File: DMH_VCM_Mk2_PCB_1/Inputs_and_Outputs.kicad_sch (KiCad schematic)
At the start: 33 parts, among them J0 Conn_01x01, J1 TS_Jack_6.35mm_Sw, J10 TS_Jack_6.35mm_Sw, J2 TS_Jack_6.35mm_Sw, J200 IDC_02x05, J3 TS_Jack_6.35mm_Sw, J4 TS_Jack_6.35mm_Sw, J5 TS_Jack_6.35mm_Sw, J50 Conn_01x06, J6 TS_Jack_6.35mm_Sw, J60 Conn_01x06, J7 TS_Jack_6.35mm_Sw, J70 Conn_01x06, J8 TS_Jack_6.35mm_Sw, J9 TS_Jack_6.35mm_Sw, SW1 SW_DPDT, SW2 SW_DPDT, SW3 SW_DPDT

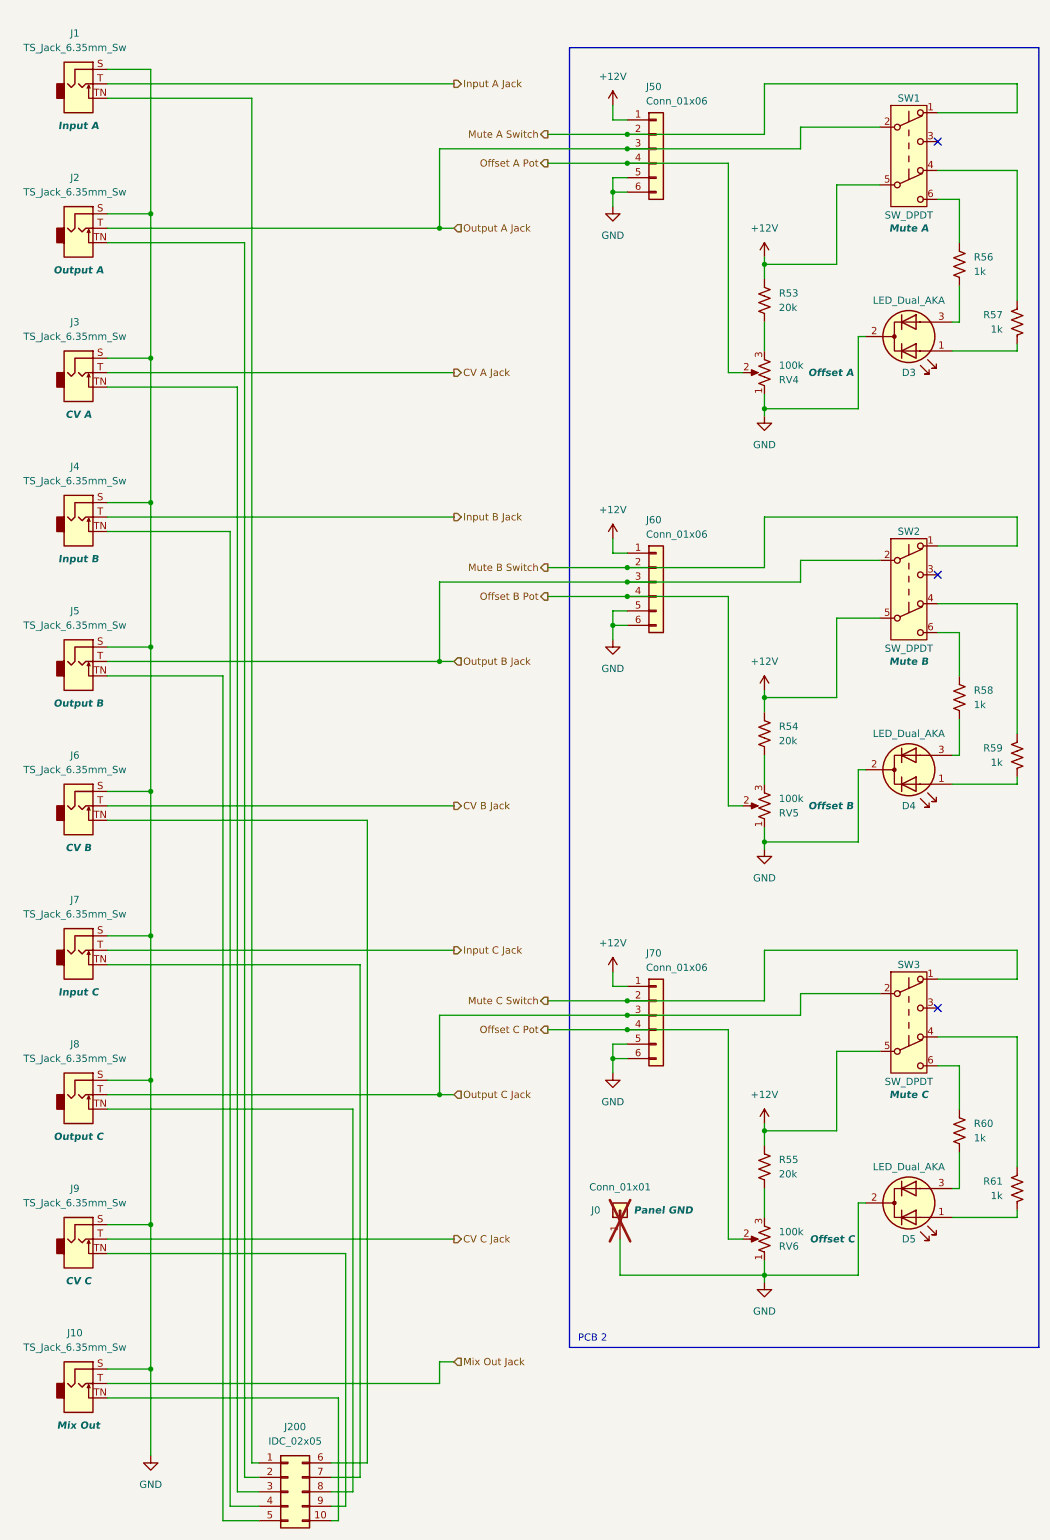
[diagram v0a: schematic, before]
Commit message: Almost finished PCB 1 schematic
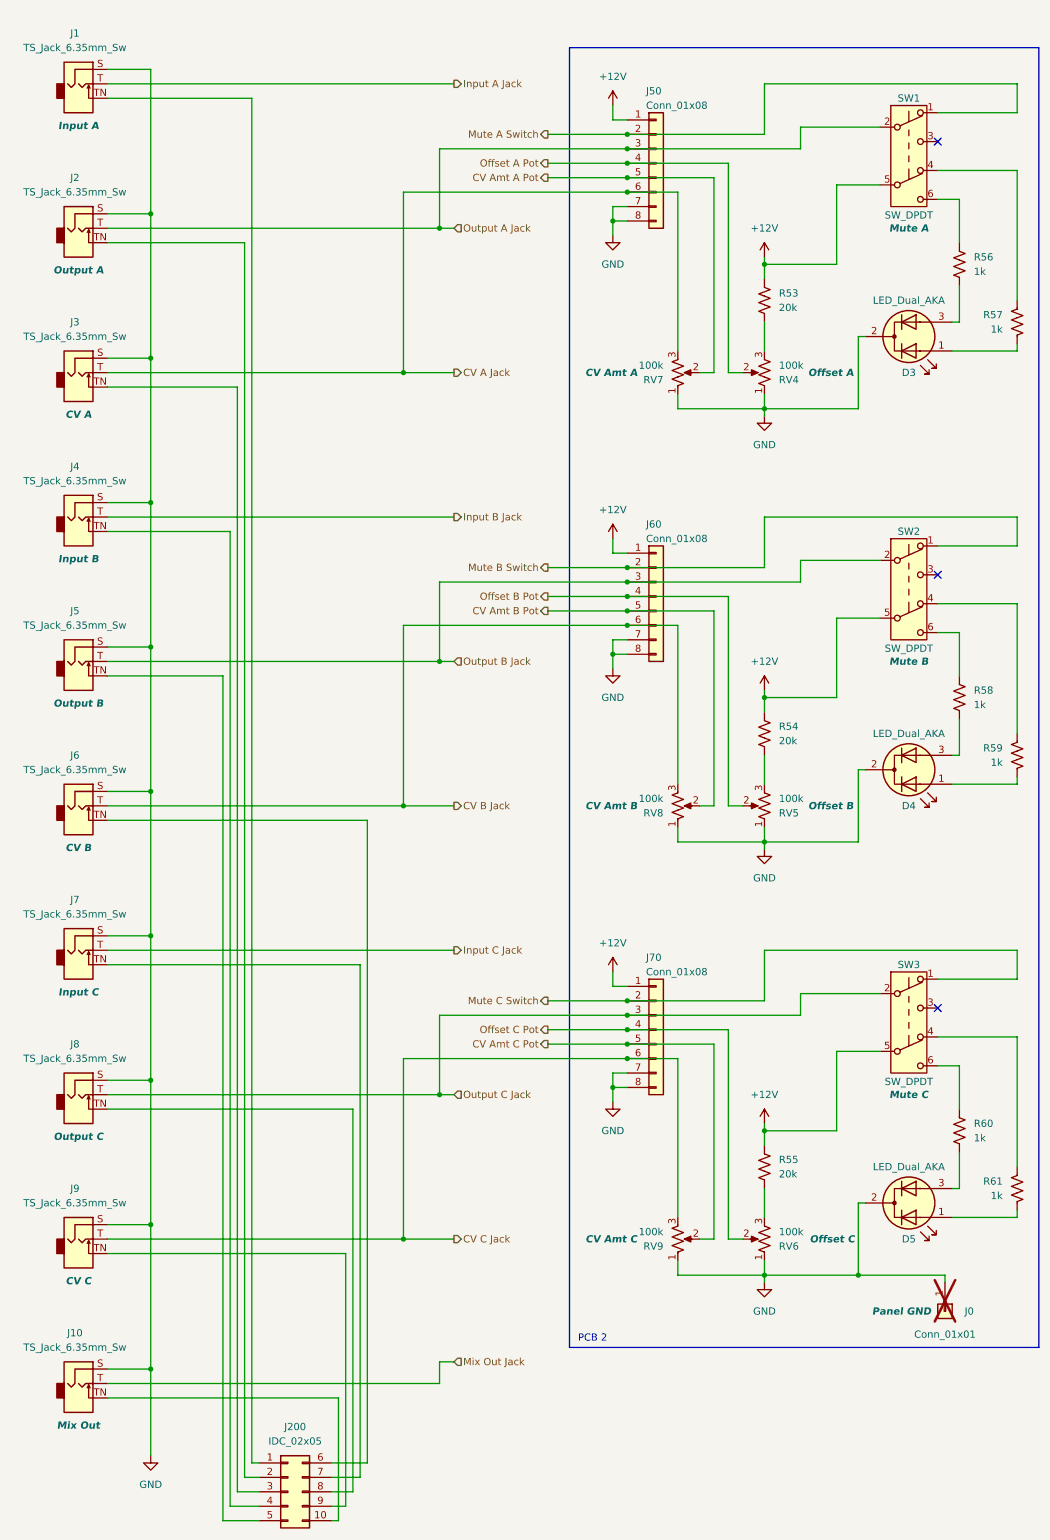
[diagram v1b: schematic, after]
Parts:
- added RV7, RV8, RV9: 100k, SynthStuff:Potentiometer_TT_P110KH1, symbol Device:R_Potentiometer_US
- J50, J60, J70: value Conn_01x06 -> Conn_01x08; symbol Connector_Generic:Conn_01x06 -> Connector_Generic:Conn_01x08
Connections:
- net CV A Jack: now also J50.6 (Pin_6), RV7.3
- net CV B Jack: now also J60.6 (Pin_6), RV8.3
- net CV C Jack: now also J70.6 (Pin_6), RV9.3
- net GND: now also J50.7 (Pin_7), J50.8 (Pin_8), J60.7 (Pin_7), J60.8 (Pin_8), J70.7 (Pin_7), J70.8 (Pin_8), RV7.1, RV8.1, RV9.1; no longer J50.5 (Pin_5), J50.6 (Pin_6), J60.5 (Pin_5), J60.6 (Pin_6), J70.5 (Pin_5), J70.6 (Pin_6)
- new net CV Amt A Pot: J50.5 (Pin_5), RV7.2
- new net CV Amt B Pot: J60.5 (Pin_5), RV8.2
- new net CV Amt C Pot: J70.5 (Pin_5), RV9.2
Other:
- moved on the sheet: J0

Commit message: PCB 1 placement in progress
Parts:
- J50, J60, J70: footprint Connector_PinSocket_2.54mm:PinSocket_1x06_P2.54mm_Vertical -> Connector_PinSocket_2.54mm:PinSocket_1x08_P2.54mm_Vertical
- SW1, SW2, SW3: footprint SynthStuff:Toggle_Switch_2_Poles_THT -> SynthStuff:Toggle_Switch_2_Poles_TE
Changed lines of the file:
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@@
 			)
 		)
-		(property "Footprint" "SynthStuff:Toggle_Switch_2_Poles_THT"
+		(property "Footprint" "SynthStuff:Toggle_Switch_2_Poles_TE"
 			(at 171.45 33.02 0)
 			(effects
@@
 			)
 		)
-		(property "Footprint" "SynthStuff:Toggle_Switch_2_Poles_THT"
+		(property "Footprint" "SynthStuff:Toggle_Switch_2_Poles_TE"
 			(at 171.45 185.42 0)
 			(effects
@@
 			)
 		)
-		(property "Footprint" "SynthStuff:Toggle_Switch_2_Poles_THT"
+		(property "Footprint" "SynthStuff:Toggle_Switch_2_Poles_TE"
 			(at 171.45 109.22 0)
 			(effects
@@
 			)
 		)
-		(property "Footprint" "Connector_PinSocket_2.54mm:PinSocket_1x06_P2.54mm_Vertical"
+		(property "Footprint" "Connector_PinSocket_2.54mm:PinSocket_1x08_P2.54mm_Vertical"
 			(at 127 115.57 0)
 			(effects
@@
 				)
 				(hide yes)
+			)
+		)
+		(property "Function" ""
+			(at 127 115.57 0)
+			(effects
+				(font
+					(size 1.27 1.27)
+				)
 			)
 		)
@@
 			)
 		)
-		(property "Footprint" "Connector_PinSocket_2.54mm:PinSocket_1x06_P2.54mm_Vertical"
+		(property "Footprint" "Connector_PinSocket_2.54mm:PinSocket_1x08_P2.54mm_Vertical"
 			(at 127 191.77 0)
 			(effects
@@
 			)
 		)
+		(property "Function" ""
+			(at 127 191.77 0)
+			(effects
+				(font
+					(size 1.27 1.27)
+				)
+			)
+		)
 		(pin "6"
 		)
@@
 			)
 		)
-		(property "Footprint" "Connector_PinSocket_2.54mm:PinSocket_1x06_P2.54mm_Vertical"
+		(property "Footprint" "Connector_PinSocket_2.54mm:PinSocket_1x08_P2.54mm_Vertical"
 			(at 127 39.37 0)
 			(effects
@@
 			)
 		)
+		(property "Function" ""
+			(at 127 39.37 0)
+			(effects
+				(font
+					(size 1.27 1.27)
+				)
+			)
+		)

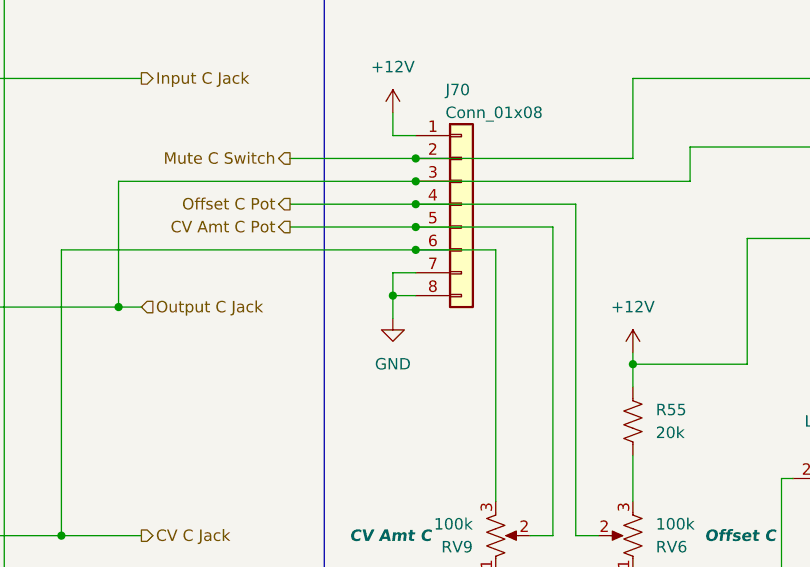
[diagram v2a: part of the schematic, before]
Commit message: Resolved J70 volume conflict
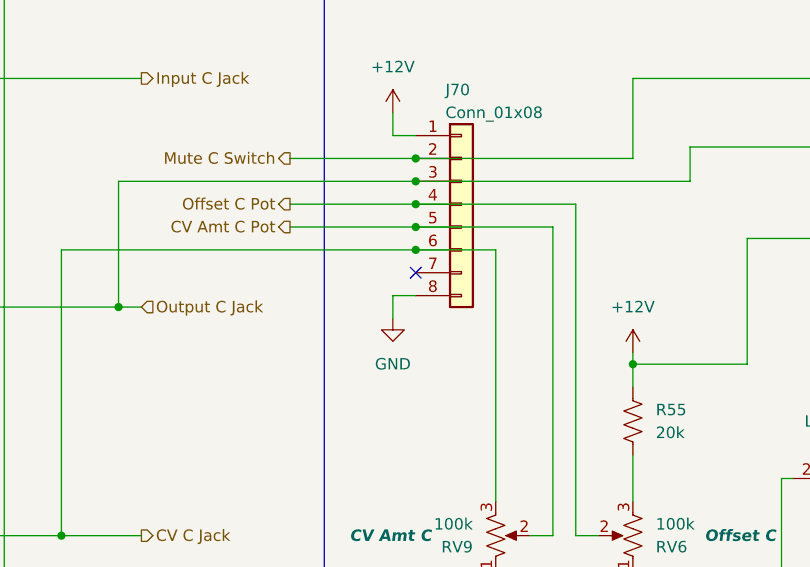
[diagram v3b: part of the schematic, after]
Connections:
- net GND: no longer J70.7 (Pin_7)
- no-connect marks 3 -> 4
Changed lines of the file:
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@@
-	)
-	(junction
-		(at 119.38 201.93)
-		(diameter 0)
-		(color 0 0 0 0)
 	)
 	(junction
@@
 		(at 176.53 35.56)
 	)
+	(no_connect
+		(at 121.92 199.39)
+	)
 	(wire
 		(pts
@@
 	(wire
 		(pts
-			(xy 119.38 199.39) (xy 119.38 201.93)
-		)
-		(stroke
-			(width 0)
-			(type default)
-		)
-	)
-	(wire
-		(pts
 			(xy 119.38 184.15) (xy 121.92 184.15)
 		)
@@
 		)
 		(stroke
-			(width 0)
-			(type default)
-		)
-	)
-	(wire
-		(pts
-			(xy 121.92 199.39) (xy 119.38 199.39)
-		)
-		(stroke

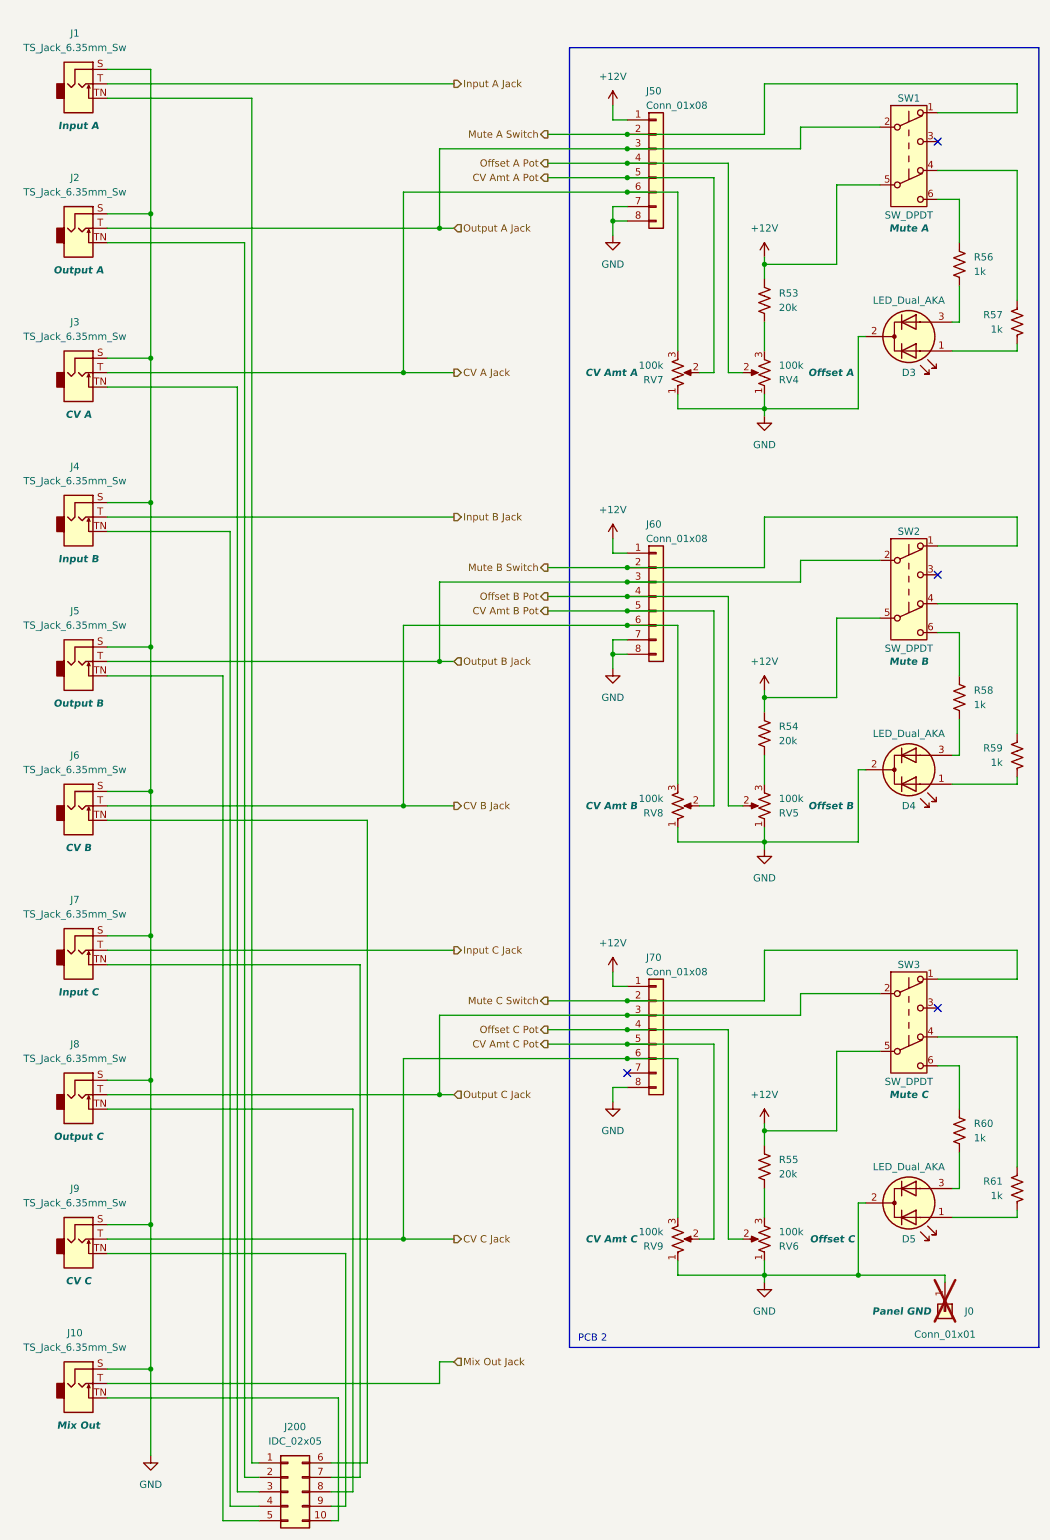
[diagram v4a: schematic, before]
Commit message: Added +/-7v5 to input TN and normalled CV inputs
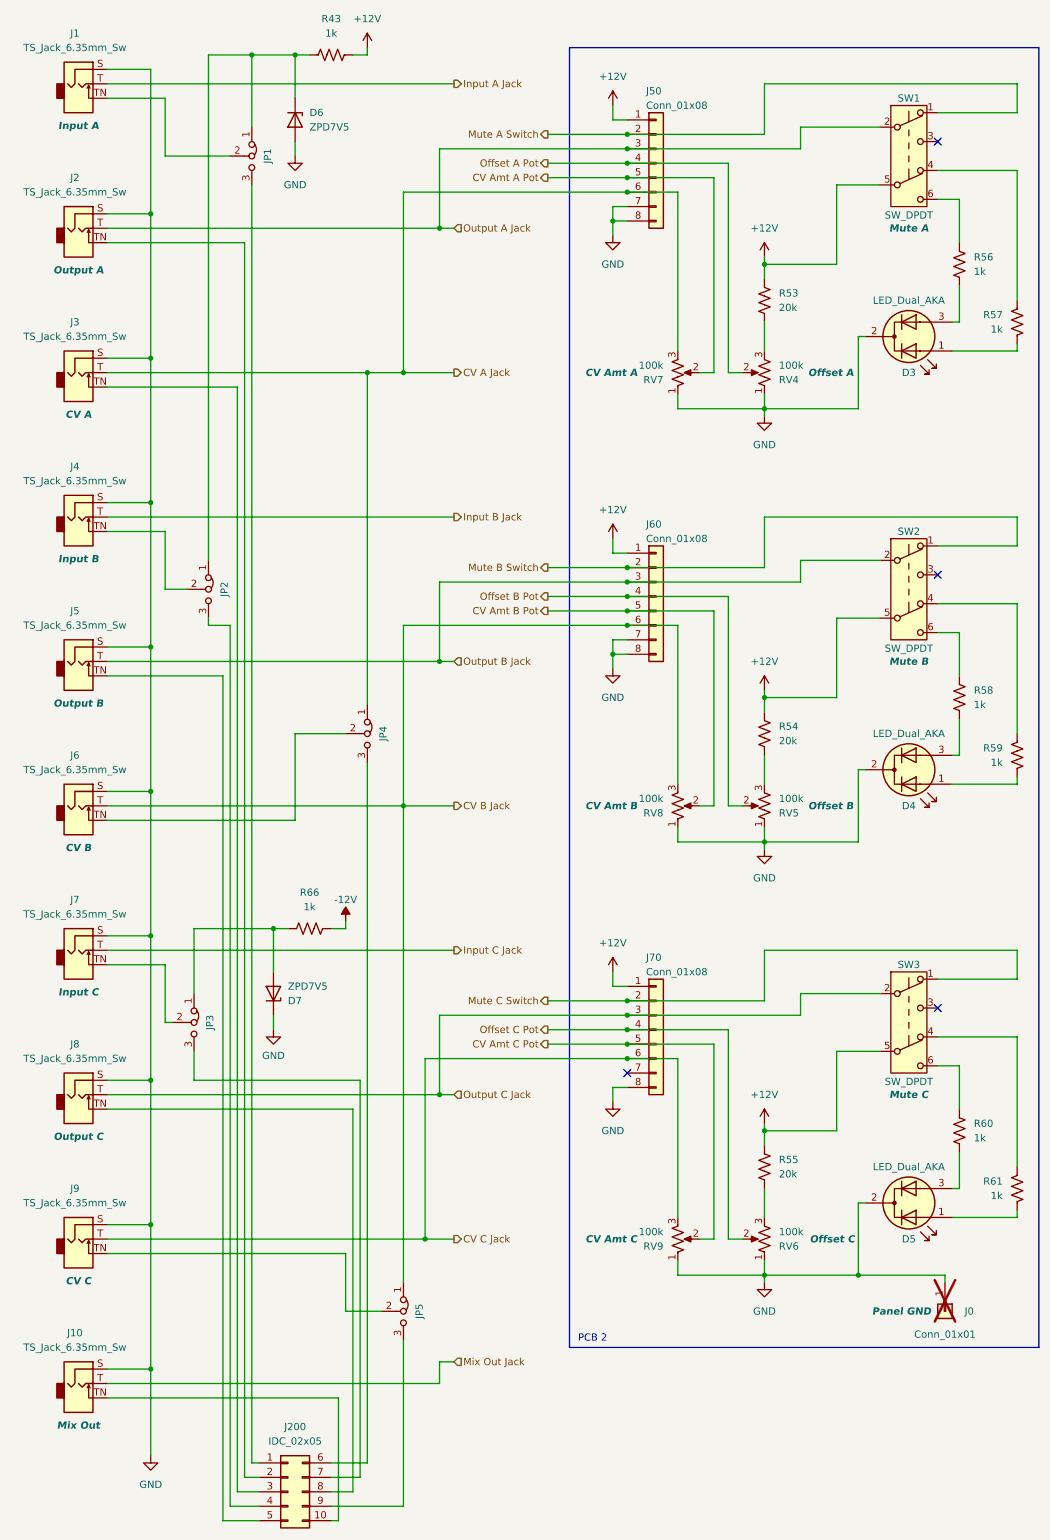
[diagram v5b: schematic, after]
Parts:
- added D6, D7: ZPD7V5, Diode_THT:D_DO-35_SOD27_P7.62mm_Horizontal, symbol Diode:ZPDxx
- added JP1, JP2, JP3, JP4, JP5: Jumper_3_Bridged12, Connector_PinHeader_2.54mm:PinHeader_1x03_P2.54mm_Vertical, symbol Jumper:Jumper_3_Bridged12
- added R43, R66: 1k, Resistor_THT:R_Axial_DIN0207_L6.3mm_D2.5mm_P2.54mm_Vertical, symbol Device:R_US
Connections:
- net +12V: now also R43.1
- net CV A Jack: now also JP4.1 (A)
- net CV B Jack: now also JP5.1 (A)
- net GND: now also D6.2 (A), D7.1 (K)
- net at J9.TN: now also JP5.2 (C); no longer J200.9 (Pin_9)
- net at J200.1 (Pin_1): now also JP1.3 (B); no longer J1.TN
- net at J200.4 (Pin_4): now also JP2.3 (B); no longer J4.TN
- net at J6.TN: now also JP4.2 (C); no longer J200.6 (Pin_6)
- net at J200.7 (Pin_7): now also JP3.3 (B); no longer J7.TN
- new net: J200.9 (Pin_9), JP5.3 (B)
- new net: J200.6 (Pin_6), JP4.3 (B)
- new net: J4.TN, JP2.2 (C)
- new net: D7.2 (A), JP3.1 (A), R66.2
- new net: J7.TN, JP3.2 (C)
- new net: D6.1 (K), JP1.1 (A), JP2.1 (A), R43.2
- new net: J1.TN, JP1.2 (C)
- new net -12V: R66.1
